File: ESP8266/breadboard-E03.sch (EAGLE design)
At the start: 11 parts, among them CON1 USBMICRO-NO_CENTER

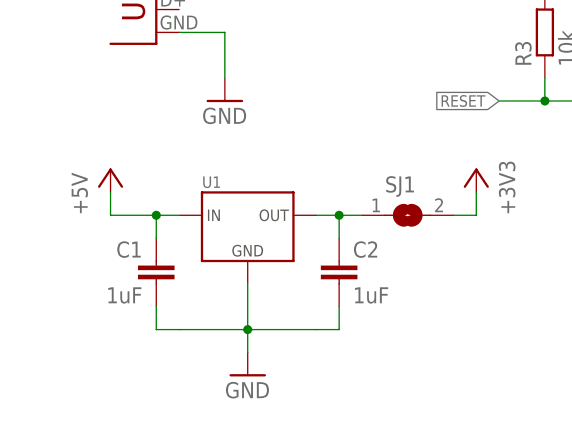
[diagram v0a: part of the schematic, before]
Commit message: switch to different vreg
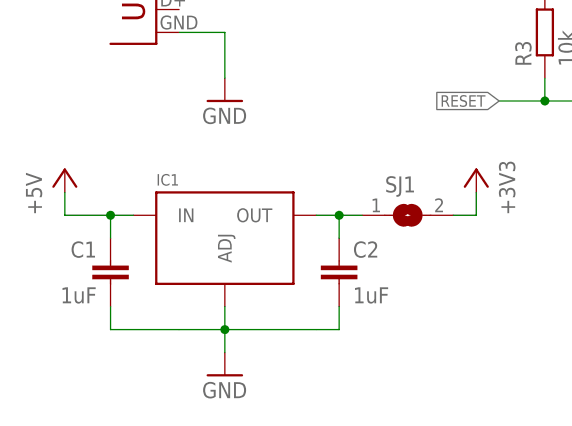
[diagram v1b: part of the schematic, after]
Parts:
- removed U1: (no value), p.peter-regulators:REGULATOR-XC6206SOT23
- added IC1: (no value), p.peter-regulators:REGULATOR-TLV1117SOT223
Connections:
- net +5V: now also IC1.IN; no longer U1.IN
- net GND: now also IC1.ADJ; no longer U1.GND
- net N$1: now also IC1.OUT; no longer U1.OUT
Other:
- moved on the sheet: C1
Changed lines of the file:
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@@
 <part name="U$1" library="p.peter-periphery" deviceset="ESP8266-03" device=""/>
 <part name="CON1" library="p.peter-connectors" deviceset="USB" device="MICRO-NO_CENTER"/>
-<part name="U1" library="p.peter-regulators" deviceset="REGULATOR-XC6206" device="SOT23"/>
 <part name="P+1" library="supply1" deviceset="+5V" device=""/>
 <part name="+3V1" library="supply1" deviceset="+3V3" device=""/>
@@
 <part name="GND6" library="supply1" deviceset="GND" device=""/>
 <part name="SJ1" library="jumper" deviceset="SJ" device=""/>
+<part name="IC1" library="p.peter-regulators" deviceset="REGULATOR-TLV1117" device="SOT223"/>
 </parts>
 <sheets>
@@
 <instance part="U$1" gate="G$1" x="43.18" y="43.18"/>
 <instance part="CON1" gate="G$1" x="-25.4" y="55.88"/>
-<instance part="U1" gate="G$1" x="-15.24" y="33.02"/>
-<instance part="P+1" gate="1" x="-30.48" y="38.1"/>
+<instance part="P+1" gate="1" x="-35.56" y="38.1"/>
 <instance part="+3V1" gate="G$1" x="10.16" y="38.1" rot="MR0"/>
-<instance part="GND1" gate="1" x="-15.24" y="15.24"/>
-<instance part="C1" gate="G$1" x="-25.4" y="27.94" rot="MR0"/>
+<instance part="GND1" gate="1" x="-17.78" y="15.24"/>
+<instance part="C1" gate="G$1" x="-30.48" y="27.94" rot="MR0"/>
 <instance part="C2" gate="G$1" x="-5.08" y="27.94"/>
 <instance part="GND2" gate="1" x="-17.78" y="45.72"/>
@@
 <instance part="GND6" gate="1" x="40.64" y="73.66"/>
 <instance part="SJ1" gate="1" x="2.54" y="33.02"/>
+<instance part="IC1" gate="1117" x="-17.78" y="30.48"/>
 </instances>
 <busses>
@@
 <segment>
 <pinref part="P+1" gate="1" pin="+5V"/>
-<pinref part="U1" gate="G$1" pin="IN"/>
-<wire x1="-22.86" y1="33.02" x2="-25.4" y2="33.02" width="0.1524" layer="91"/>
-<wire x1="-25.4" y1="33.02" x2="-30.48" y2="33.02" width="0.1524" layer="91"/>
-<wire x1="-30.48" y1="33.02" x2="-30.48" y2="35.56" width="0.1524" layer="91"/>
+<wire x1="-27.94" y1="33.02" x2="-30.48" y2="33.02" width="0.1524" layer="91"/>
+<wire x1="-30.48" y1="33.02" x2="-35.56" y2="33.02" width="0.1524" layer="91"/>
+<wire x1="-35.56" y1="33.02" x2="-35.56" y2="35.56" width="0.1524" layer="91"/>
 <pinref part="C1" gate="G$1" pin="1"/>
-<wire x1="-25.4" y1="30.48" x2="-25.4" y2="33.02" width="0.1524" layer="91"/>
-<junction x="-25.4" y="33.02"/>
+<wire x1="-30.48" y1="30.48" x2="-30.48" y2="33.02" width="0.1524" layer="91"/>
+<junction x="-30.48" y="33.02"/>
+<pinref part="IC1" gate="1117" pin="IN"/>
 </segment>
 <segment>
@@
 <net name="GND" class="0">
 <segment>
-<pinref part="U1" gate="G$1" pin="GND"/>
 <pinref part="GND1" gate="1" pin="GND"/>
-<wire x1="-15.24" y1="17.78" x2="-15.24" y2="20.32" width="0.1524" layer="91"/>
+<wire x1="-17.78" y1="17.78" x2="-17.78" y2="20.32" width="0.1524" layer="91"/>
 <pinref part="C1" gate="G$1" pin="2"/>
-<wire x1="-15.24" y1="20.32" x2="-15.24" y2="25.4" width="0.1524" layer="91"/>
-<wire x1="-25.4" y1="22.86" x2="-25.4" y2="20.32" width="0.1524" layer="91"/>
-<wire x1="-25.4" y1="20.32" x2="-22.86" y2="20.32" width="0.1524" layer="91"/>
-<wire x1="-22.86" y1="20.32" x2="-15.24" y2="20.32" width="0.1524" layer="91"/>
-<wire x1="-15.24" y1="20.32" x2="-7.62" y2="20.32" width="0.1524" layer="91"/>
+<wire x1="-17.78" y1="20.32" x2="-17.78" y2="22.86" width="0.1524" layer="91"/>
+<wire x1="-30.48" y1="22.86" x2="-30.48" y2="20.32" width="0.1524" layer="91"/>
+<wire x1="-30.48" y1="20.32" x2="-22.86" y2="20.32" width="0.1524" layer="91"/>
+<wire x1="-22.86" y1="20.32" x2="-17.78" y2="20.32" width="0.1524" layer="91"/>
+<wire x1="-17.78" y1="20.32" x2="-7.62" y2="20.32" width="0.1524" layer="91"/>
 <pinref part="C2" gate="G$1" pin="2"/>
 <wire x1="-7.62" y1="20.32" x2="-5.08" y2="20.32" width="0.1524" layer="91"/>
 <wire x1="-5.08" y1="20.32" x2="-5.08" y2="22.86" width="0.1524" layer="91"/>
-<junction x="-15.24" y="20.32"/>
+<junction x="-17.78" y="20.32"/>
+<pinref part="IC1" gate="1117" pin="ADJ"/>
 </segment>
 <segment>
@@
 <net name="N$1" class="0">
 <segment>
-<pinref part="U1" gate="G$1" pin="OUT"/>
 <wire x1="-2.54" y1="33.02" x2="-5.08" y2="33.02" width="0.1524" layer="91"/>
 <wire x1="-5.08" y1="33.02" x2="-7.62" y2="33.02" width="0.1524" layer="91"/>
@@
 <junction x="-5.08" y="33.02"/>
 <pinref part="SJ1" gate="1" pin="1"/>
-</segment>
-</net>
+<pinref part="IC1" gate="1117" pin="OUT"/>
+</segment>
+</net>
